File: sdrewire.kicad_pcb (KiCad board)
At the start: 4 copper layers, 31 x 23.6 mm, 99 parts, among them J1 USB_C_Receptacle, J2 Conn_01x06, J3 Micro_SD_Card, J4 uSD_edge_contacts, Q1 DMG1032UV, Q2 DMG1013UW, Q3 DMG1032UV, U1 MIC5363-3.3YMT, U11 SN74LVC1G14DRL, U12 TS3DDR4000ZBAR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

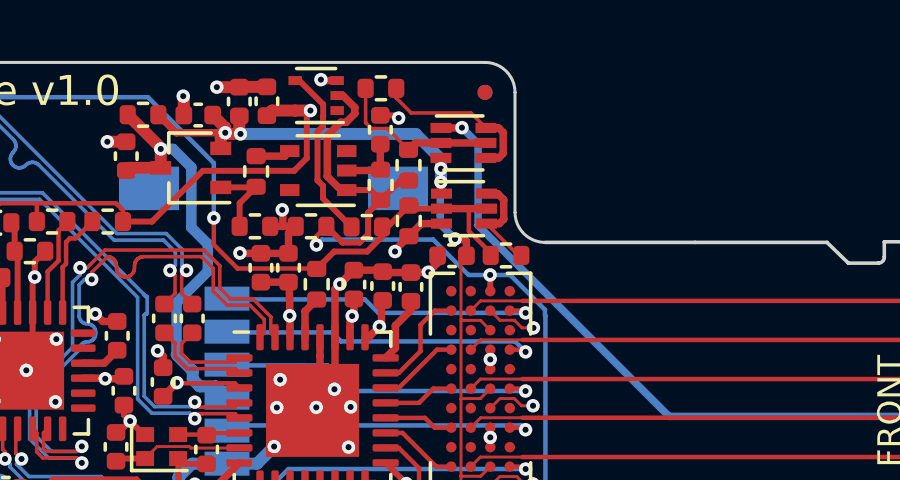
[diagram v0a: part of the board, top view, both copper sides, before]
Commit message: SDReWire: fix back-to-back transistors circuit
Signed-off-by: Dominik Sliwa <dominik@sliwa.io>
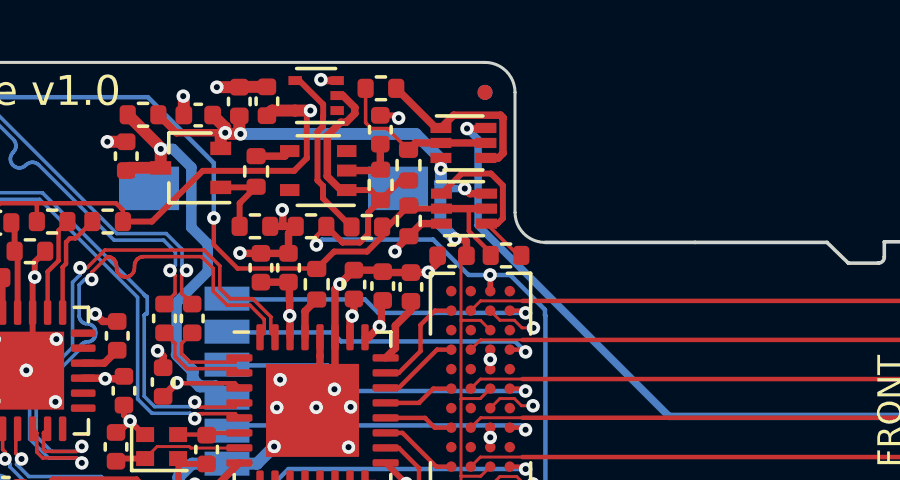
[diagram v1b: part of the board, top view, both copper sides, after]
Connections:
- Q1 pad 1: /SD/SD_{MUX}_V_{DD} -> Net-(Q1-Pad1)
- Q1 pad 4: Net-(Q1-Pad4) -> Net-(Q1-Pad1)
- Q1 pad 6: Net-(Q1-Pad4) -> /SD/SD_{MUX}_V_{DD}
- Q3 pad 1: /SD/EXT_V_{DD} -> Net-(Q3-Pad1)
- Q3 pad 4: Net-(Q3-Pad4) -> Net-(Q3-Pad1)
- Q3 pad 6: Net-(Q3-Pad4) -> /SD/EXT_V_{DD}
- R10 pad 2: Net-(Q1-Pad4) -> Net-(Q1-Pad1)
- R9 pad 2: Net-(Q3-Pad4) -> Net-(Q3-Pad1)
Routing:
- net Net-(Q3-Pad1): track 0.00 -> 6.14 mm
- net Net-(Q1-Pad1): track 0.00 -> 5.80 mm
- net Net-(Q3-Pad4): track 5.70 -> 0.00 mm
- net Net-(Q1-Pad4): track 3.54 -> 0.00 mm
- net /SD/SD_{MUX}_V_{DD}: track 29.6 -> 30.9 mm

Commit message: Changes:
-fix led order
-fix transistor routing
-modify usb hub strapping and fix crystal footprint
-remove copper under sd pads
-routing cleanup
-change revision to 1.1

Signed-off-by: Dominik Sliwa <dominik@sliwa.io>
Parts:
- removed R11: DNI, Resistor_SMD:R_0402_1005Metric
- removed R2: 100k, Resistor_SMD:R_0402_1005Metric
- removed R8: 47k, Resistor_SMD:R_0402_1005Metric
- C15, C19, C20, C4: value 6pF -> 22pF
- C44: value 4.7uF -> 0.1uF
- C48: footprint Capacitor_SMD:C_0201_0603Metric -> Capacitor_SMD:C_0402_1005Metric
- Q1, Q3: value DMG1032UV -> DMG1023UV
- R10, R4, R5, R9: value 47k -> 100k
- R37: value 4k7 -> 1k
- R39: value 4k7 -> 10k
- moved R1 1.96 mm to (131.8, 91.2)
- moved R4 1.58 mm to (133.2, 89.6), turned to -90 degrees
- moved R5 1.35 mm to (131.8, 90.2)
- moved C55 0.30 mm to (142.7, 91.6)
- moved C48 0.21 mm to (138.4, 99.0)
- moved C15 0.19 mm to (128.6, 97.4), turned to 0 degrees
- moved C49 0.10 mm to (143.9, 91.7)
- moved C56 0.07 mm to (144.8, 91.7)
- turned Y1 to 180 degrees
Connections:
- net /FTDI_USB2_D+ renamed /FTDI/FTDI_USB2_D+
- net /FTDI_USB2_D- renamed /FTDI/FTDI_USB2_D-
- net /GL_USB2_D+ renamed /SD/GL_USB2_D+
- net /GL_USB2_D- renamed /SD/GL_USB2_D-
- net /GL_USB3_RX+ renamed /SD/GL_USB3_RX+
- net /GL_USB3_RX- renamed /SD/GL_USB3_RX-
- net /GL_USB3_TX+ renamed /SD/GL_USB3_TX+
- net /GL_USB3_TX- renamed /SD/GL_USB3_TX-
- net /SD_MUX_SEL renamed /FTDI/SD_MUX_SEL
- net /UFP_USB2_D+ renamed /USB HUB/UFP_USB2_D+
- net /UFP_USB2_D- renamed /USB HUB/UFP_USB2_D-
- J1 pad A8: (no net) -> unconnected-(J1-PadA8)
- J1 pad B8: (no net) -> unconnected-(J1-PadB8)
- R1 pad 1: Net-(R1-Pad1) -> GND
- R1 pad 2: +5V -> Net-(U4-Pad17)
- R26 pad 2: /SD/GL_V_{DD} -> /SD/SD_{MUX}_V_{DD}
- R5 pad 1: +3V3 -> GND
- RN1 pad 3: Net-(D4-Pad2) -> Net-(D3-Pad2)
- RN1 pad 4: Net-(D3-Pad2) -> Net-(D4-Pad2)
- RN1 pad 5: +3V3 -> /SD/~SD_MUX_SEL
- RN1 pad 6: /SD/~SD_MUX_SEL -> +3V3
- U1 pad 1: (no net) -> unconnected-(U1-Pad1)
- U1 pad 2: (no net) -> unconnected-(U1-Pad2)
- U11 pad 1: (no net) -> unconnected-(U11-Pad1)
- U12 pad B1: (no net) -> unconnected-(U12-PadB1)
- U12 pad B3: (no net) -> unconnected-(U12-PadB3)
- U12 pad B4: (no net) -> unconnected-(U12-PadB4)
- U12 pad D1: (no net) -> unconnected-(U12-PadD1)
- U12 pad D3: (no net) -> unconnected-(U12-PadD3)
- U12 pad D4: (no net) -> unconnected-(U12-PadD4)
- U12 pad F1: (no net) -> unconnected-(U12-PadF1)
- U12 pad F3: (no net) -> unconnected-(U12-PadF3)
- U12 pad F4: (no net) -> unconnected-(U12-PadF4)
- U12 pad H1: (no net) -> unconnected-(U12-PadH1)
- U12 pad H3: (no net) -> unconnected-(U12-PadH3)
- U12 pad H4: (no net) -> unconnected-(U12-PadH4)
- U12 pad K1: (no net) -> unconnected-(U12-PadK1)
- U12 pad K3: (no net) -> unconnected-(U12-PadK3)
- U12 pad K4: (no net) -> unconnected-(U12-PadK4)
- U12 pad M1: (no net) -> unconnected-(U12-PadM1)
- U12 pad M3: (no net) -> unconnected-(U12-PadM3)
- U12 pad M4: (no net) -> unconnected-(U12-PadM4)
- U13 pad 3: (no net) -> unconnected-(U13-Pad3)
- U13 pad 5: (no net) -> unconnected-(U13-Pad5)
- U2 pad 22: (no net) -> unconnected-(U2-Pad22)
- U2 pad 23: (no net) -> unconnected-(U2-Pad23)
- U2 pad 24: (no net) -> unconnected-(U2-Pad24)
- U2 pad 25: (no net) -> unconnected-(U2-Pad25)
- U2 pad 26: (no net) -> unconnected-(U2-Pad26)
- U2 pad 27: (no net) -> unconnected-(U2-Pad27)
- U2 pad 3: (no net) -> unconnected-(U2-Pad3)
- U3 pad 12: (no net) -> unconnected-(U3-Pad12)
- U3 pad 14: (no net) -> unconnected-(U3-Pad14)
- U3 pad 16: (no net) -> unconnected-(U3-Pad16)
- U3 pad 18: (no net) -> unconnected-(U3-Pad18)
- U3 pad 19: (no net) -> unconnected-(U3-Pad19)
- U4 pad 11: (no net) -> unconnected-(U4-Pad11)
- U4 pad 12: (no net) -> unconnected-(U4-Pad12)
- U4 pad 15: GND -> +3V3
- U4 pad 16: Net-(R1-Pad1) -> +3V3
- U4 pad 17: Net-(R8-Pad2) -> Net-(U4-Pad17)
- U4 pad 23: (no net) -> unconnected-(U4-Pad23)
- U4 pad 7: (no net) -> unconnected-(U4-Pad7)
- U4 pad 8: (no net) -> unconnected-(U4-Pad8)
- U7 pad 16: (no net) -> unconnected-(U7-Pad16)
- U7 pad 4: (no net) -> unconnected-(U7-Pad4)
- Y1 pad 1: GND -> Net-(C15-Pad2)
- Y1 pad 2: Net-(C15-Pad2) -> GND
- Y1 pad 3: GND -> Net-(C4-Pad2)
- Y1 pad 4: Net-(C4-Pad2) -> GND
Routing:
- net +3V3: track 103.6 -> 111.3 mm, vias 11 -> 9
- net Net-(C47-Pad2): track 25.4 -> 21.4 mm, vias 4 -> 2
- net Net-(R1-Pad1): track 3.08 -> 0.00 mm
- net +5V: track 70.4 -> 68.8 mm
- net /SD/SD_V_{DD}: track 14.0 -> 12.5 mm
- net Net-(D3-Pad2): track 1.27 -> 2.71 mm
- net /SD/~SD_MUX_SEL: track 39.1 -> 37.7 mm, vias 3 -> 2
- net Net-(C52-Pad2): track 20.5 -> 21.8 mm
- net Net-(U4-Pad17): track 0.00 -> 1.19 mm
- net Net-(R8-Pad2): track 1.17 -> 0.00 mm
- net Net-(R4-Pad2): track 3.55 -> 2.52 mm
- net Net-(R5-Pad2): track 3.31 -> 2.47 mm
- net /SD/SD_{MUX}_V_{DD}: track 30.9 -> 30.2 mm, vias 5 -> 4
- net Net-(Q3-Pad1): track 6.14 -> 6.71 mm
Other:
- outline, holes or cut-outs redrawn
- board text added: "SDReWire v1.1"
- board text removed: "SDReWire v1.0"

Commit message: PCB: traces cleanup
Signed-off-by: Dominik Sliwa <dominik@sliwa.io>
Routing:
- net Net-(C52-Pad2): track 21.8 -> 19.9 mm
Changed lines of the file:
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@@
   (via (at 137.030928 94.771268) (size 0.45) (drill 0.2) (layers "F.Cu" "B.Cu") (remove_unused_layers) (keep_end_layers) (net 36))
   (via (at 145.55 99.474999) (size 0.45) (drill 0.2) (layers "F.Cu" "B.Cu") (net 36))
-  (segment (start 137.628732 94.771268) (end 137.030928 94.771268) (width 0.25) (layer "In2.Cu") (net 36))
-  (segment (start 138.41 95.08) (end 138.1 94.77) (width 0.25) (layer "In2.Cu") (net 36))
-  (segment (start 138.1 94.77) (end 137.63 94.77) (width 0.25) (layer "In2.Cu") (net 36))
-  (segment (start 138.41 96.52) (end 138.41 95.08) (width 0.25) (layer "In2.Cu") (net 36))
+  (segment (start 138.25 99.9) (end 138.25 95.1) (width 0.25) (layer "In2.Cu") (net 36))
   (segment (start 145.375001 99.474999) (end 144.489999 100.360001) (width 0.2) (layer "In2.Cu") (net 36))
+  (segment (start 138.25 95.1) (end 137.921268 94.771268) (width 0.25) (layer "In2.Cu") (net 36))
+  (segment (start 137.921268 94.771268) (end 137.030928 94.771268) (width 0.25) (layer "In2.Cu") (net 36))
   (segment (start 145.55 99.474999) (end 145.375001 99.474999) (width 0.2) (layer "In2.Cu") (net 36))
-  (segment (start 136.629999 98.756001) (end 136.629999 98.300001) (width 0.25) (layer "In2.Cu") (net 36))
   (segment (start 144.489999 100.360001) (end 142.447499 100.360001) (width 0.2) (layer "In2.Cu") (net 36))
-  (segment (start 138.233999 100.360001) (end 136.629999 98.756001) (width 0.25) (layer "In2.Cu") (net 36))
-  (segment (start 142.447499 100.360001) (end 138.233999 100.360001) (width 0.25) (layer "In2.Cu") (net 36))
-  (segment (start 136.629999 98.300001) (end 138.41 96.52) (width 0.25) (layer "In2.Cu") (net 36))
-  (segment (start 137.63 94.77) (end 137.628732 94.771268) (width 0.25) (layer "In2.Cu") (net 36))
+  (segment (start 142.447499 100.360001) (end 138.710001 100.360001) (width 0.25) (layer "In2.Cu") (net 36))
+  (segment (start 138.710001 100.360001) (end 138.25 99.9) (width 0.25) (layer "In2.Cu") (net 36))
   (segment (start 144.83 92.35) (end 144.31 92.87) (width 0.25) (layer "F.Cu") (net 37))
   (segment (start 144.31 93.6225) (end 143.9875 93.945) (width 0.25) (layer "F.Cu") (net 37))
